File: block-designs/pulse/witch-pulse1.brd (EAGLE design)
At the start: 134.6 x 64.4 mm, 30 parts, among them IC1 NE555, IC2 74LS73N, IC3 74S08N, IC4 7432N, J1 POWER_JACKPTH

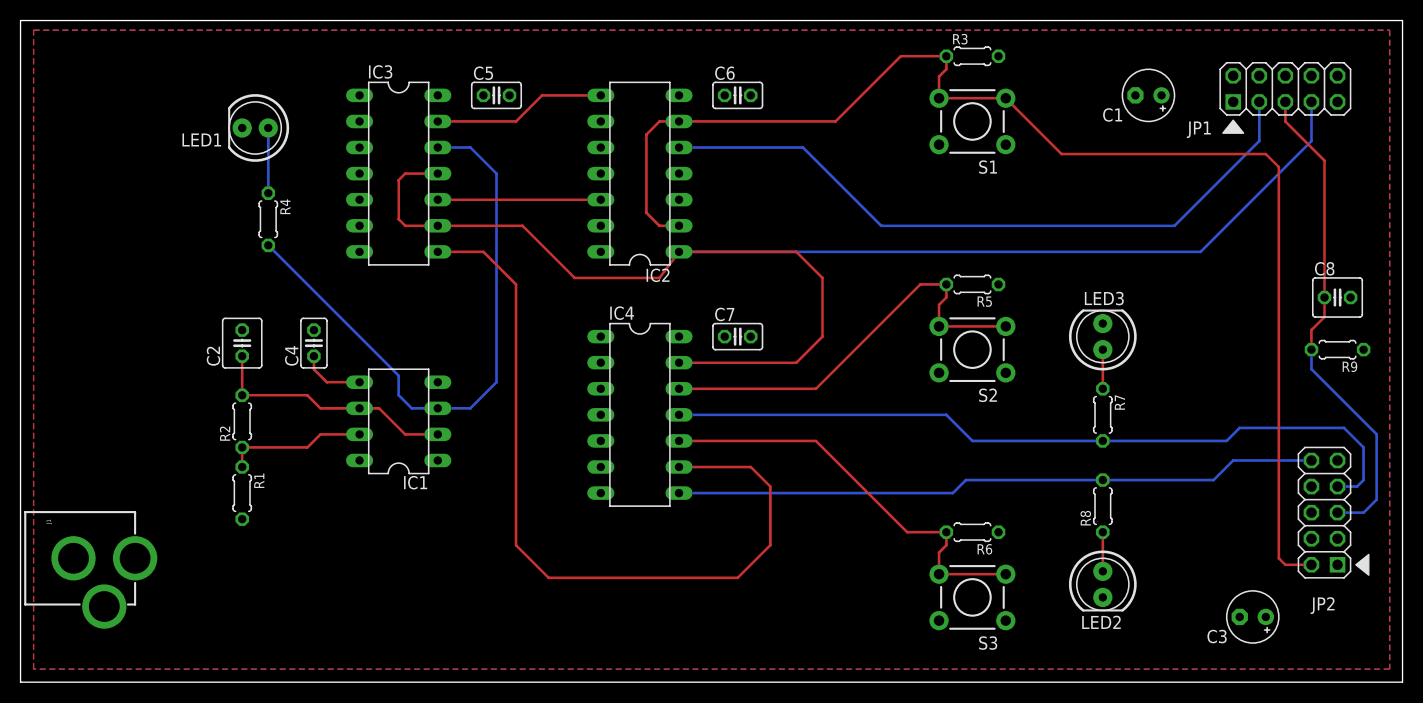
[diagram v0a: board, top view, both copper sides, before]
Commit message: updated dekatron layout
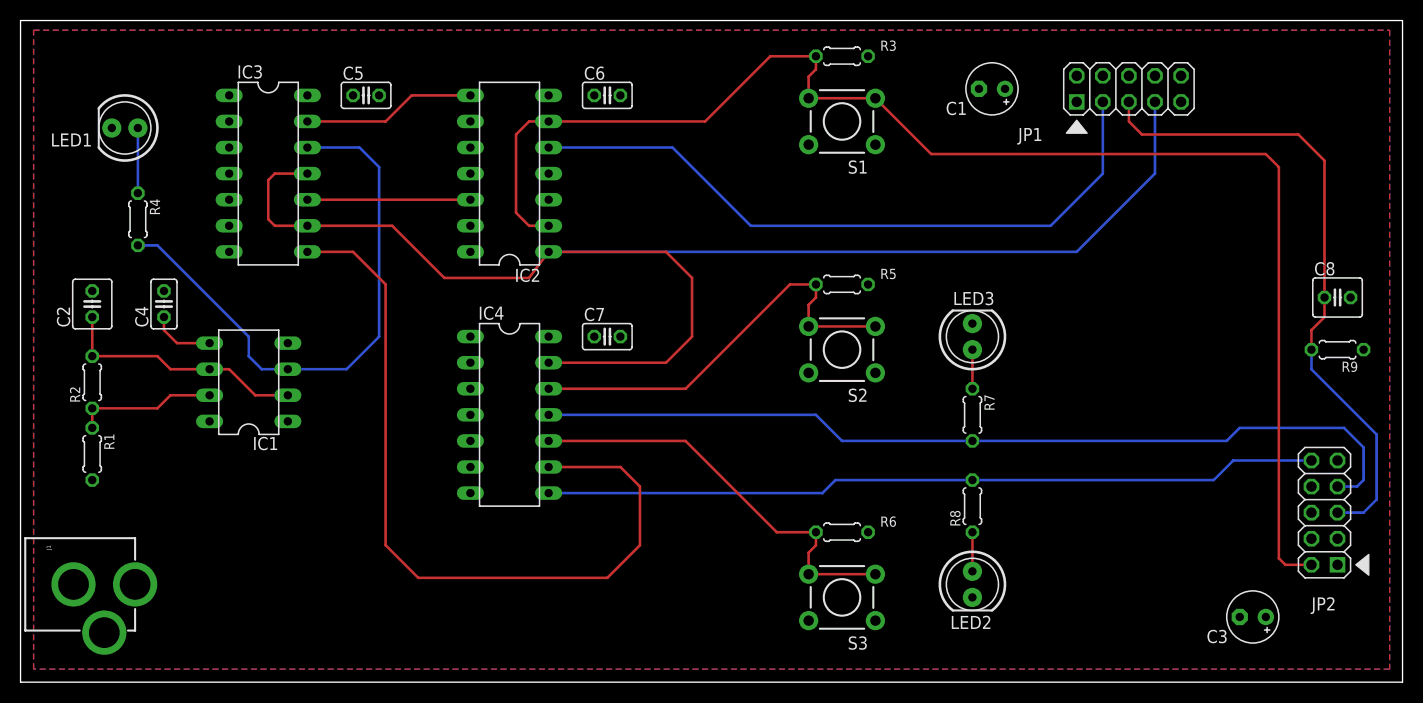
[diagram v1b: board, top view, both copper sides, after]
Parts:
- moved C1 15.3 mm to (94.6, 57.8)
- moved JP1 15.2 mm to (108.0, 57.8)
- moved C2 15.1 mm to (6.99, 36.8)
- moved IC1 15.1 mm to (22.2, 29.2)
- moved R1 15.1 mm to (6.99, 22.2)
- moved R2 15.1 mm to (6.99, 29.2)
- moved C4 15.1 mm to (14.0, 36.8)
- moved IC2 12.7 mm to (47.6, 49.5)
- moved IC4 12.7 mm to (47.6, 26.0)
- moved LED2 12.7 mm to (92.7, 9.53)
- moved LED3 12.7 mm to (92.7, 33.7)
- moved R7 12.7 mm to (92.7, 26.0)
- moved R8 12.7 mm to (92.7, 17.1)
- moved IC3 12.7 mm to (24.1, 49.5)
- moved LED1 12.7 mm to (10.2, 54.0)
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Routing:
- net DK_RESET: track 47.8 -> 63.0 mm
- net RESET: track 125.5 -> 138.2 mm
- net N$4: track 62.9 -> 75.6 mm
- net N$19: track 75.0 -> 87.7 mm
- net N$2: track 58.1 -> 55.2 mm
- net N$12: track 66.9 -> 66.2 mm
- net 10A_PULSE: track 144.5 -> 143.8 mm

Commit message: updated pdf schematics and board files with fixes
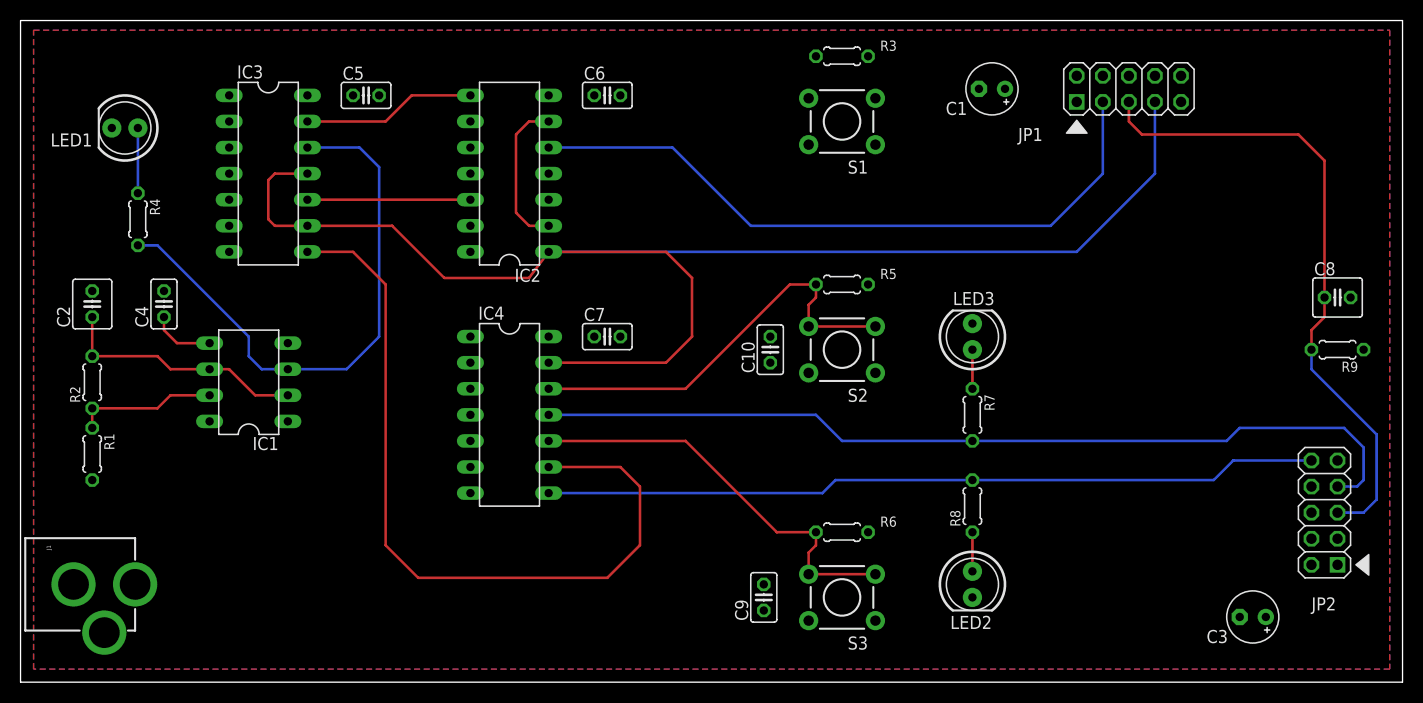
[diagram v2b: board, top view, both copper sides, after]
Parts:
- added C10, C9: (no value), resistor:C025-025X050
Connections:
- new net N$1: IC4.2, R3.1, S1.3, S1.4
- new net VDD1: C10.1
- net N$2: now also IC4.1
- net N$6: now also C10.2
- net N$9: now also C9.2
- net RESET: now also IC4.3; no longer R3.1, S1.3, S1.4
- net VDD: now also C9.1
- net VSS: now also J1.GND
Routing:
- net RESET: track 138.2 -> 15.0 mm
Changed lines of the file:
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@@
 <element name="R9" library="resistor" package="0204/5" value="" x="128.27" y="32.385" rot="R180"/>
 <element name="C8" library="resistor" package="C025-040X050" value="" x="128.27" y="37.465"/>
+<element name="C9" library="resistor" package="C025-025X050" value="" x="72.39" y="8.255" rot="R90"/>
+<element name="C10" library="resistor" package="C025-025X050" value="" x="73.025" y="32.385" rot="R90"/>
 </elements>
 <signals>
@@
 <wire x1="22.225" y1="31.75" x2="23.495" y2="30.48" width="0.254" layer="16"/>
 <wire x1="23.495" y1="30.48" x2="26.035" y2="30.48" width="0.254" layer="16"/>
+<contactref element="IC4" pad="1"/>
+<wire x1="34.925" y1="33.655" x2="43.815" y2="33.655" width="0" layer="19" extent="16-16"/>
 </signal>
 <signal name="N$7">
@@
 <wire x1="27.94" y1="46.99" x2="43.815" y2="46.99" width="0.254" layer="1"/>
 </signal>
-<signal name="VDD">
+<signal name="VDD" airwireshidden="yes">
 <contactref element="IC3" pad="14"/>
 <contactref element="IC4" pad="14"/>
@@
 <contactref element="J1" pad="PWR"/>
 <contactref element="R9" pad="1"/>
+<contactref element="C9" pad="1"/>
+<wire x1="128.27" y1="11.43" x2="130.81" y2="32.385" width="0" layer="19" extent="1-1"/>
+<wire x1="121.285" y1="6.35" x2="128.27" y2="11.43" width="0" layer="19" extent="1-1"/>
+<wire x1="102.87" y1="56.515" x2="130.81" y2="32.385" width="0" layer="19" extent="1-1"/>
+<wire x1="95.885" y1="57.785" x2="102.87" y2="56.515" width="0" layer="19" extent="1-1"/>
+<wire x1="82.55" y1="60.96" x2="95.885" y2="57.785" width="0" layer="19" extent="1-1"/>
+<wire x1="55.88" y1="57.15" x2="82.55" y2="60.96" width="0" layer="19" extent="1-1"/>
+<wire x1="51.435" y1="57.15" x2="55.88" y2="57.15" width="0" layer="19" extent="1-1"/>
+<wire x1="51.435" y1="49.53" x2="51.435" y2="57.15" width="0" layer="19" extent="1-1"/>
+<wire x1="43.815" y1="41.91" x2="51.435" y2="49.53" width="0" layer="19" extent="1-1"/>
+<wire x1="51.435" y1="33.655" x2="43.815" y2="41.91" width="0" layer="19" extent="1-1"/>
+<wire x1="55.88" y1="33.655" x2="51.435" y2="33.655" width="0" layer="19" extent="1-1"/>
+<wire x1="32.385" y1="57.15" x2="51.435" y2="57.15" width="0" layer="19" extent="1-1"/>
+<wire x1="27.94" y1="57.15" x2="32.385" y2="57.15" width="0" layer="19" extent="1-1"/>
+<wire x1="26.035" y1="33.02" x2="43.815" y2="41.91" width="0" layer="19" extent="1-1"/>
+<wire x1="18.415" y1="25.4" x2="26.035" y2="33.02" width="0" layer="19" extent="1-1"/>
+<wire x1="6.985" y1="19.685" x2="18.415" y2="25.4" width="0" layer="19" extent="1-1"/>
+<wire x1="11.16" y1="9.525" x2="6.985" y2="19.685" width="0" layer="19" extent="1-1"/>
+<wire x1="72.39" y1="6.985" x2="11.16" y2="9.525" width="0" layer="19" extent="1-1"/>
+<wire x1="76.7588" y1="30.1244" x2="55.88" y2="33.655" width="0" layer="19" extent="1-1"/>
+<wire x1="83.2612" y1="30.1244" x2="76.7588" y2="30.1244" width="0" layer="19" extent="1-1"/>
+<wire x1="83.2612" y1="5.9944" x2="83.2612" y2="30.1244" width="0" layer="19" extent="1-1"/>
+<wire x1="76.7588" y1="5.9944" x2="83.2612" y2="5.9944" width="0" layer="19" extent="1-1"/>
 </signal>
 <signal name="N$6">
@@
 <wire x1="77.47" y1="37.465" x2="77.47" y2="38.735" width="0.254" layer="1"/>
 <wire x1="76.7588" y1="34.6456" x2="83.2612" y2="34.6456" width="0.254" layer="1"/>
+<contactref element="C10" pad="2"/>
+<wire x1="73.025" y1="33.655" x2="51.435" y2="28.575" width="0" layer="19" extent="1-1"/>
 </signal>
 <signal name="N$9">
@@
 <wire x1="64.77" y1="23.495" x2="73.66" y2="14.605" width="0.254" layer="1"/>
 <wire x1="73.66" y1="14.605" x2="77.47" y2="14.605" width="0.254" layer="1"/>
-</signal>
-<signal name="VSS">
+<contactref element="C9" pad="2"/>
+<wire x1="72.39" y1="9.525" x2="51.435" y2="23.495" width="0" layer="19" extent="1-1"/>
+</signal>
+<signal name="VSS" airwireshidden="yes">
 <contactref element="IC3" pad="7"/>
 <contactref element="IC4" pad="7"/>
@@
 <contactref element="J1" pad="GNDBREAK"/>
 <contactref element="C8" pad="2"/>
+<contactref element="J1" pad="GND"/>
+<wire x1="93.345" y1="57.785" x2="113.03" y2="56.515" width="0" layer="19" extent="1-1"/>
+<wire x1="83.2612" y1="52.3494" x2="93.345" y2="57.785" width="0" layer="19" extent="1-1"/>
+<wire x1="76.7588" y1="52.3494" x2="83.2612" y2="52.3494" width="0" layer="19" extent="1-1"/>
+<wire x1="82.55" y1="38.735" x2="83.2612" y2="52.3494" width="0" layer="19" extent="1-1"/>
+<wire x1="92.71" y1="34.925" x2="82.55" y2="38.735" width="0" layer="19" extent="1-1"/>
+<wire x1="58.42" y1="57.15" x2="76.7588" y2="52.3494" width="0" layer="19" extent="1-1"/>
+<wire x1="51.435" y1="46.99" x2="58.42" y2="57.15" width="0" layer="19" extent="1-1"/>
+<wire x1="43.815" y1="49.53" x2="51.435" y2="46.99" width="0" layer="19" extent="1-1"/>
+<wire x1="43.815" y1="52.07" x2="43.815" y2="49.53" width="0" layer="19" extent="1-1"/>
+<wire x1="34.925" y1="57.15" x2="43.815" y2="52.07" width="0" layer="19" extent="1-1"/>
+<wire x1="58.42" y1="33.655" x2="51.435" y2="46.99" width="0" layer="19" extent="1-1"/>
+<wire x1="20.32" y1="41.91" x2="34.925" y2="57.15" width="0" layer="19" extent="1-1"/>
+<wire x1="13.97" y1="38.1" x2="20.32" y2="41.91" width="0" layer="19" extent="1-1"/>
+<wire x1="6.985" y1="38.1" x2="13.97" y2="38.1" width="0" layer="19" extent="1-1"/>
+<wire x1="8.89" y1="53.975" x2="6.985" y2="38.1" width="0" layer="19" extent="1-1"/>
+<wire x1="26.035" y1="25.4" x2="20.32" y2="41.91" width="0" layer="19" extent="1-1"/>
+<wire x1="43.815" y1="18.415" x2="26.035" y2="25.4" width="0" layer="19" extent="1-1"/>
+<wire x1="82.55" y1="14.605" x2="92.71" y2="34.925" width="0" layer="19" extent="1-1"/>
+<wire x1="92.71" y1="8.255" x2="82.55" y2="14.605" width="0" layer="19" extent="1-1"/>
+<wire x1="129.54" y1="37.465" x2="113.03" y2="56.515" width="0" layer="19" extent="1-1"/>
+<wire x1="128.27" y1="21.59" x2="129.54" y2="37.465" width="0" layer="19" extent="1-1"/>
+<wire x1="118.745" y1="6.35" x2="128.27" y2="21.59" width="0" layer="19" extent="1-1"/>
+<wire x1="5.16" y1="9.525" x2="26.035" y2="25.4" width="0" layer="19" extent="1-1"/>
+<wire x1="8.16" y1="4.825" x2="5.16" y2="9.525" width="0" layer="19" extent="1-1"/>
 </signal>
 <signal name="RESET">
@@
 <wire x1="49.53" y1="44.45" x2="51.435" y2="44.45" width="0.254" layer="1"/>
 <contactref element="IC2" pad="6"/>
-<wire x1="51.435" y1="54.61" x2="66.675" y2="54.61" width="0.254" layer="1"/>
-<wire x1="73.025" y1="60.96" x2="66.675" y2="54.61" width="0.254" layer="1"/>
-<contactref element="S1" pad="4"/>
-<contactref element="S1" pad="3"/>
-<contactref element="R3" pad="1"/>
-<wire x1="76.7588" y1="56.8706" x2="76.7588" y2="58.9788" width="0.254" layer="1"/>
-<wire x1="76.7588" y1="58.9788" x2="77.47" y2="59.69" width="0.254" layer="1"/>
-<wire x1="76.7588" y1="56.8706" x2="83.2612" y2="56.8706" width="0.254" layer="1"/>
-<wire x1="73.025" y1="60.96" x2="77.47" y2="60.96" width="0.254" layer="1"/>
-<wire x1="77.47" y1="59.69" x2="77.47" y2="60.96" width="0.254" layer="1"/>
 <wire x1="49.53" y1="54.61" x2="51.435" y2="54.61" width="0.254" layer="1"/>
-<wire x1="125.73" y1="11.43" x2="123.19" y2="11.43" width="0.254" layer="1"/>
-<wire x1="123.19" y1="11.43" x2="122.555" y2="12.065" width="0.254" layer="1"/>
-<wire x1="122.555" y1="12.065" x2="122.555" y2="50.165" width="0.254" layer="1"/>
-<wire x1="122.555" y1="50.165" x2="121.285" y2="51.435" width="0.254" layer="1"/>
-<wire x1="121.285" y1="51.435" x2="88.6968" y2="51.435" width="0.254" layer="1"/>
-<wire x1="88.6968" y1="51.435" x2="83.2612" y2="56.8706" width="0.254" layer="1"/>
+<contactref element="IC4" pad="3"/>
+<wire x1="51.435" y1="44.45" x2="125.73" y2="11.43" width="0" layer="19" extent="1-1"/>
+<wire x1="43.815" y1="28.575" x2="49.53" y2="44.45" width="0" layer="19" extent="1-1"/>
 </signal>
 <signal name="N$12">
@@
 <wire x1="107.95" y1="54.61" x2="107.95" y2="56.515" width="0.254" layer="1"/>
 </signal>
+<signal name="VDD1">
+<contactref element="C10" pad="1"/>
+</signal>
+<signal name="N$1">
+<contactref element="S1" pad="4"/>
+<contactref element="IC4" pad="2"/>
+<contactref element="S1" pad="3"/>
+<contactref element="R3" pad="1"/>
+<wire x1="76.7588" y1="56.8706" x2="83.2612" y2="56.8706" width="0" layer="19" extent="1-1"/>
+<wire x1="77.47" y1="60.96" x2="76.7588" y2="56.8706" width="0" layer="19" extent="1-1"/>
+<wire x1="43.815" y1="31.115" x2="76.7588" y2="56.8706" width="0" layer="19" extent="1-1"/>
+</signal>
 </signals>
